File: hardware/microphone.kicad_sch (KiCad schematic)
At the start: 15 parts

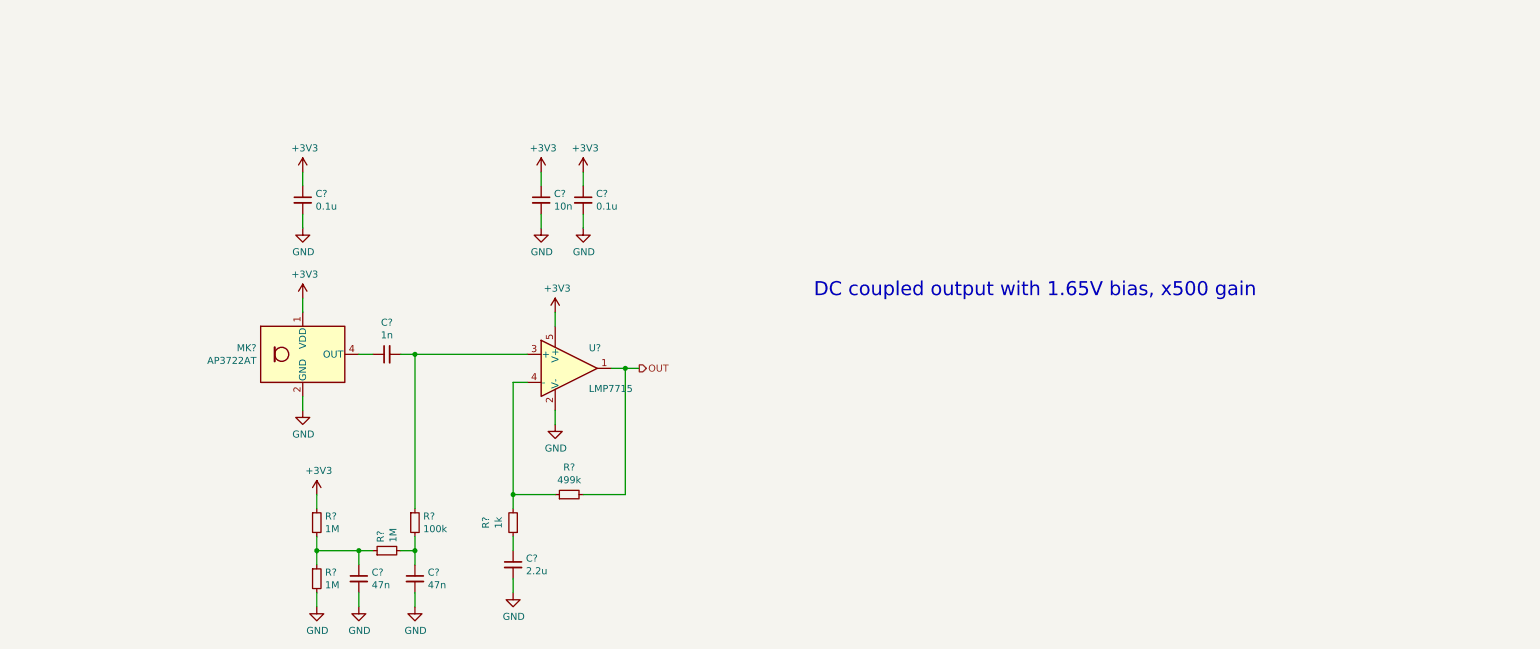
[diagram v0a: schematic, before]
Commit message: Simulate amplification circuit and adjust values accordingly
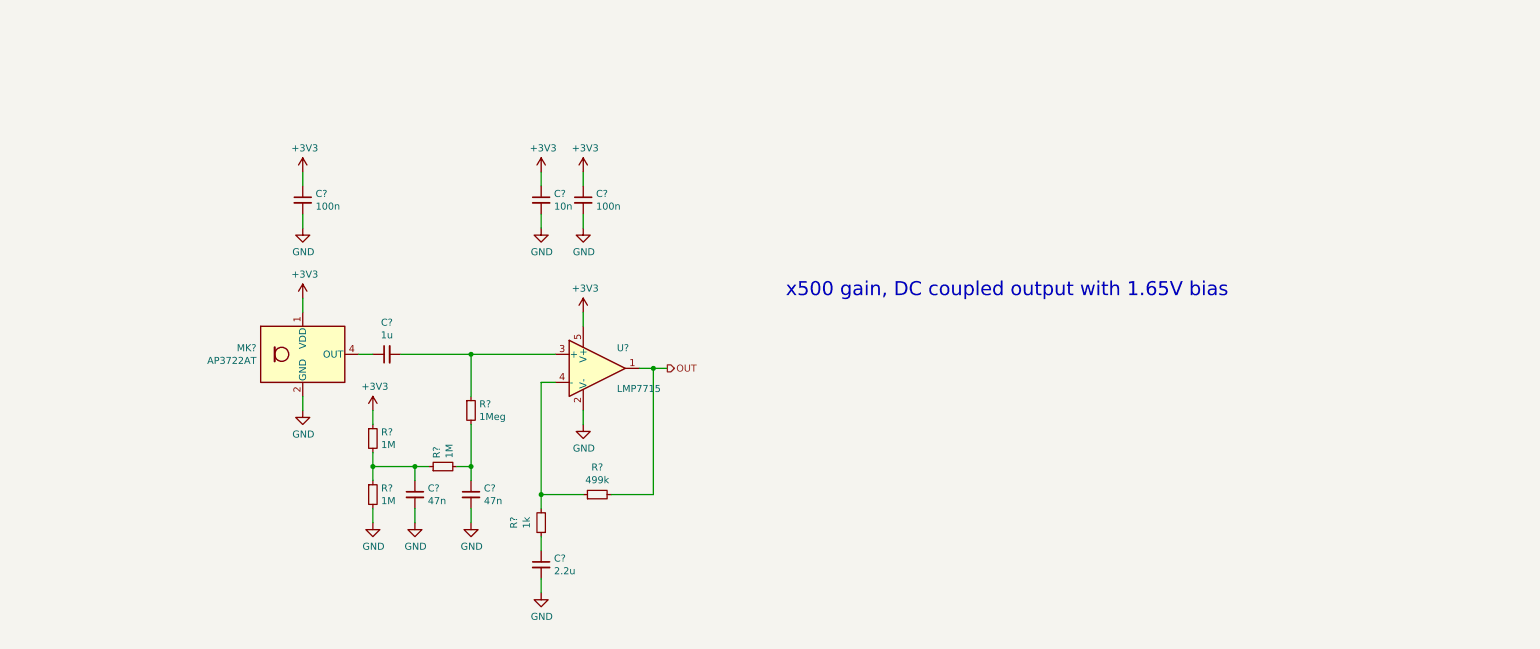
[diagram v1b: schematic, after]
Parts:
- C? (x2): value 0.1u -> 100n; Dielectric (none) -> -; Tolerance (none) -> 10%; Voltage (none) -> 6.3V
- C?: value 1n -> 1u; Dielectric (none) -> -; Tolerance (none) -> 10%; Voltage (none) -> 6.3V
- C? (x4): Dielectric (none) -> -; Tolerance (none) -> 10%; Voltage (none) -> 6.3V
- R? (x5): Tolerance (none) -> 1%; Voltage (none) -> 50V
- R?: value 100k -> 1Meg; Tolerance (none) -> 1%; Voltage (none) -> 50V
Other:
- note added: "x500 gain, DC coupled output with 1.65V bias"
- note removed: "DC coupled output with 1.65V bias, x500 gain"
- moved on the sheet: C?, R?, U?

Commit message: Cleanup schematic, connect usb
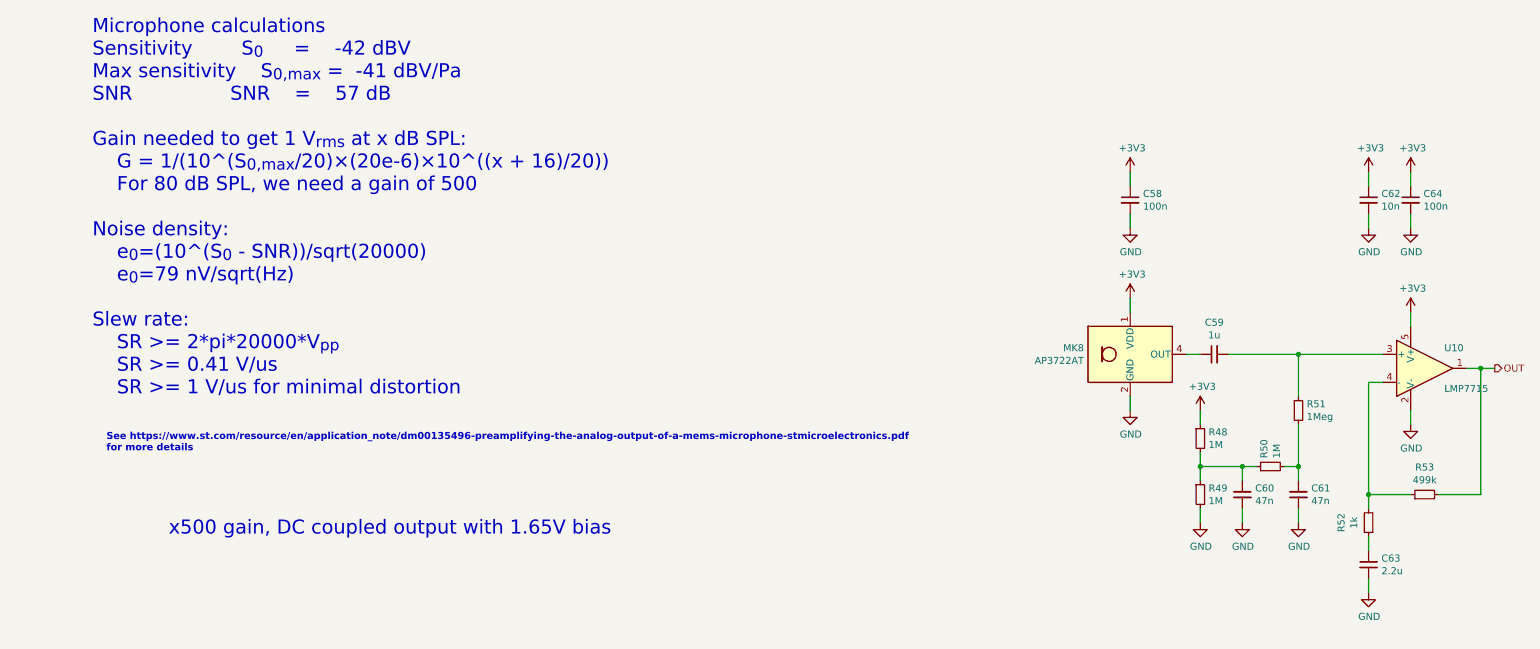
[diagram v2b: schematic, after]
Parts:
- gave numbers to parts that had none: 15
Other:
- note added: "Microphone calculations Sensitivity S_{0} = -42 dBV Max sensitivity S_{0,max} = -41 dBV/Pa SNR SNR = 57 dB Gain needed to get 1 V_{rms} at x dB SPL: G = 1/(10^(S_{0,max}/20)×(20e-6)×10^((x + 16)/20)) For 80 dB SPL, we need a gain of 500 Noise density: e_{0}=(10^(S_{0} - SNR))/sqrt(20000) e_{0}=79 nV/sqrt(Hz) Slew rate: SR >= 2*pi*20000*V_{pp} SR >= 0.41 V/us SR >= 1 V/us for minimal distortion"
- note added: "See https://www.st.com/resource/en/application_note/dm00135496-preamplifying-the-analog-output-of-a-mems-microphone-stmicroelectronics.pdf for more details"
- moved on the sheet: C58, C59, C60, C61, C62, C63, C64, MK8, R48, R49, R50, R51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

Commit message: Assign footprints
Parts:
- C58, C64: footprint (none) -> Capacitor_SMD:C_0402_1005Metric; Dielectric - -> X7R; MPN (none) -> 885012205018; Voltage 6.3V -> 10V
- C59: footprint (none) -> Capacitor_SMD:C_0402_1005Metric; Dielectric - -> X5R; MPN (none) -> CL05A105KQ5NNNC
- C60, C61: footprint (none) -> Capacitor_SMD:C_0402_1005Metric; Dielectric - -> X7R; MPN (none) -> 885012205016; Voltage 6.3V -> 10V
- C62: footprint (none) -> Capacitor_SMD:C_0402_1005Metric; Dielectric - -> X7R; MPN (none) -> 885012205031
- C63: footprint (none) -> Capacitor_SMD:C_0402_1005Metric; Dielectric - -> X7R; MPN (none) -> CL05A225MQ5NNNC; Tolerance 10% -> 20%
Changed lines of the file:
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@@
       (effects (font (size 1.27 1.27)) (justify left))
     )
-    (property "Footprint" "" (id 2) (at 205.74 50.8 0)
+    (property "Footprint" "Capacitor_SMD:C_0402_1005Metric" (id 2) (at 205.74 50.8 0)
       (effects (font (size 1.27 1.27)) hide)
     )
@@
       (effects (font (size 1.27 1.27)) hide)
     )
-    (property "Dielectric" "-" (id 4) (at 205.74 50.8 0)
+    (property "Dielectric" "X7R" (id 4) (at 205.74 50.8 0)
       (effects (font (size 1.27 1.27)) hide)
     )
-    (property "Voltage" "6.3V" (id 5) (at 205.74 50.8 0)
+    (property "Voltage" "10V" (id 5) (at 205.74 50.8 0)
       (effects (font (size 1.27 1.27)) hide)
     )
     (property "Tolerance" "10%" (id 6) (at 205.74 50.8 0)
+      (effects (font (size 1.27 1.27)) hide)
+    )
+    (property "MPN" "885012205018" (id 4) (at 205.74 50.8 0)
       (effects (font (size 1.27 1.27)) hide)
     )
@@
     (property "Reference" "C59" (id 0) (at 220.98 72.9677 90))
     (property "Value" "1u" (id 1) (at 220.98 75.2602 90))
-    (property "Footprint" "" (id 2) (at 220.98 78.74 0)
+    (property "Footprint" "Capacitor_SMD:C_0402_1005Metric" (id 2) (at 220.98 78.74 0)
       (effects (font (size 1.27 1.27)) hide)
     )
@@
       (effects (font (size 1.27 1.27)) hide)
     )
-    (property "Dielectric" "-" (id 4) (at 220.98 78.74 0)
+    (property "Dielectric" "X5R" (id 4) (at 220.98 78.74 0)
+      (effects (font (size 1.27 1.27)) hide)
+    )
+    (property "MPN" "CL05A105KQ5NNNC" (id 4) (at 220.98 78.74 0)
       (effects (font (size 1.27 1.27)) hide)
     )
@@
       (effects (font (size 1.27 1.27)) (justify left))
     )
-    (property "Footprint" "" (id 2) (at 226.06 104.14 0)
+    (property "Footprint" "Capacitor_SMD:C_0402_1005Metric" (id 2) (at 226.06 104.14 0)
       (effects (font (size 1.27 1.27)) hide)
     )
@@
       (effects (font (size 1.27 1.27)) hide)
     )
-    (property "Voltage" "6.3V" (id 5) (at 226.06 104.14 0)
+    (property "Voltage" "10V" (id 5) (at 226.06 104.14 0)
       (effects (font (size 1.27 1.27)) hide)
     )
-    (property "Dielectric" "-" (id 4) (at 226.06 104.14 0)
+    (property "Dielectric" "X7R" (id 4) (at 226.06 104.14 0)
+      (effects (font (size 1.27 1.27)) hide)
+    )
+    (property "MPN" "885012205016" (id 4) (at 226.06 104.14 0)
       (effects (font (size 1.27 1.27)) hide)
     )
@@
       (effects (font (size 1.27 1.27)) (justify left))
     )
-    (property "Footprint" "" (id 2) (at 236.22 104.14 0)
+    (property "Footprint" "Capacitor_SMD:C_0402_1005Metric" (id 2) (at 236.22 104.14 0)
       (effects (font (size 1.27 1.27)) hide)
     )
@@
       (effects (font (size 1.27 1.27)) hide)
     )
-    (property "Voltage" "6.3V" (id 5) (at 236.22 104.14 0)
+    (property "Voltage" "10V" (id 5) (at 236.22 104.14 0)
       (effects (font (size 1.27 1.27)) hide)
     )
-    (property "Dielectric" "-" (id 4) (at 236.22 104.14 0)
+    (property "Dielectric" "X7R" (id 4) (at 236.22 104.14 0)
+      (effects (font (size 1.27 1.27)) hide)
+    )
+    (property "MPN" "885012205016" (id 4) (at 236.22 104.14 0)
       (effects (font (size 1.27 1.27)) hide)
     )
@@
       (effects (font (size 1.27 1.27)) (justify left))
     )
-    (property "Footprint" "" (id 2) (at 248.92 50.8 0)
+    (property "Footprint" "Capacitor_SMD:C_0402_1005Metric" (id 2) (at 248.92 50.8 0)
       (effects (font (size 1.27 1.27)) hide)
     )
@@
       (effects (font (size 1.27 1.27)) hide)
     )
-    (property "Dielectric" "-" (id 4) (at 248.92 50.8 0)
+    (property "Dielectric" "X7R" (id 4) (at 248.92 50.8 0)
+      (effects (font (size 1.27 1.27)) hide)
+    )
+    (property "MPN" "885012205031" (id 4) (at 248.92 50.8 0)
       (effects (font (size 1.27 1.27)) hide)
     )
@@
       (effects (font (size 1.27 1.27)) (justify left))
     )
-    (property "Footprint" "" (id 2) (at 248.92 116.84 0)
+    (property "Footprint" "Capacitor_SMD:C_0402_1005Metric" (id 2) (at 248.92 116.84 0)
       (effects (font (size 1.27 1.27)) hide)
     )
@@
       (effects (font (size 1.27 1.27)) hide)
     )
-    (property "Tolerance" "10%" (id 4) (at 248.92 116.84 0)
+    (property "Tolerance" "20%" (id 4) (at 248.92 116.84 0)
       (effects (font (size 1.27 1.27)) hide)
     )
@@
       (effects (font (size 1.27 1.27)) hide)
     )
-    (property "Dielectric" "-" (id 4) (at 248.92 116.84 0)
+    (property "Dielectric" "X7R" (id 4) (at 248.92 116.84 0)
+      (effects (font (size 1.27 1.27)) hide)
+    )
+    (property "MPN" "CL05A225MQ5NNNC" (id 4) (at 248.92 116.84 0)
       (effects (font (size 1.27 1.27)) hide)
     )
@@
       (effects (font (size 1.27 1.27)) (justify left))
     )
-    (property "Footprint" "" (id 2) (at 256.54 50.8 0)
+    (property "Footprint" "Capacitor_SMD:C_0402_1005Metric" (id 2) (at 256.54 50.8 0)
       (effects (font (size 1.27 1.27)) hide)
     )
@@
       (effects (font (size 1.27 1.27)) hide)
     )
-    (property "Voltage" "6.3V" (id 5) (at 256.54 50.8 0)
+    (property "Voltage" "10V" (id 5) (at 256.54 50.8 0)
       (effects (font (size 1.27 1.27)) hide)
     )
-    (property "Dielectric" "-" (id 4) (at 256.54 50.8 0)
+    (property "Dielectric" "X7R" (id 4) (at 256.54 50.8 0)
       (effects (font (size 1.27 1.27)) hide)
     )
+    (property "MPN" "885012205018" (id 4) (at 256.54 50.8 0)
+      (effects (font (size 1.27 1.27)) hide)
+    )

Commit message: Assign all footprints
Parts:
- R48, R49, R50, R51, R52, R53: footprint (none) -> Resistor_SMD:R_0402_1005Metric
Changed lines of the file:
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@@
       (effects (font (size 1.27 1.27)) (justify left))
     )
-    (property "Footprint" "" (id 2) (at 218.44 93.98 0)
+    (property "Footprint" "Resistor_SMD:R_0402_1005Metric" (id 2) (at 218.44 93.98 0)
       (effects (font (size 1.27 1.27)) hide)
     )
@@
       (effects (font (size 1.27 1.27)) (justify left))
     )
-    (property "Footprint" "" (id 2) (at 218.44 104.14 0)
+    (property "Footprint" "Resistor_SMD:R_0402_1005Metric" (id 2) (at 218.44 104.14 0)
       (effects (font (size 1.27 1.27)) hide)
     )
@@
       (effects (font (size 1.27 1.27)) (justify left))
     )
-    (property "Footprint" "" (id 2) (at 231.14 99.06 0)
+    (property "Footprint" "Resistor_SMD:R_0402_1005Metric" (id 2) (at 231.14 99.06 0)
       (effects (font (size 1.27 1.27)) hide)
     )
@@
       (effects (font (size 1.27 1.27)) (justify left))
     )
-    (property "Footprint" "" (id 2) (at 236.22 88.9 0)
+    (property "Footprint" "Resistor_SMD:R_0402_1005Metric" (id 2) (at 236.22 88.9 0)
       (effects (font (size 1.27 1.27)) hide)
     )
@@
     (property "Reference" "R52" (id 0) (at 243.9732 109.22 90))
     (property "Value" "1k" (id 1) (at 246.2784 109.22 90))
-    (property "Footprint" "" (id 2) (at 248.92 109.22 0)
+    (property "Footprint" "Resistor_SMD:R_0402_1005Metric" (id 2) (at 248.92 109.22 0)
       (effects (font (size 1.27 1.27)) hide)
     )
@@
     (property "Reference" "R53" (id 0) (at 259.08 99.1932 90))
     (property "Value" "499k" (id 1) (at 259.08 101.4984 90))
-    (property "Footprint" "" (id 2) (at 259.08 104.14 0)
+    (property "Footprint" "Resistor_SMD:R_0402_1005Metric" (id 2) (at 259.08 104.14 0)
       (effects (font (size 1.27 1.27)) hide)
     )
